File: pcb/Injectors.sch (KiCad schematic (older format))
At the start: 48 parts, among them Q1 VND14NV04, Q2 VND14NV04, Q3 VND14NV04, Q4 VND14NV04, Q5 VND14NV04, Q6 VND14NV04, Q7 VND14NV04, Q8 VND14NV04

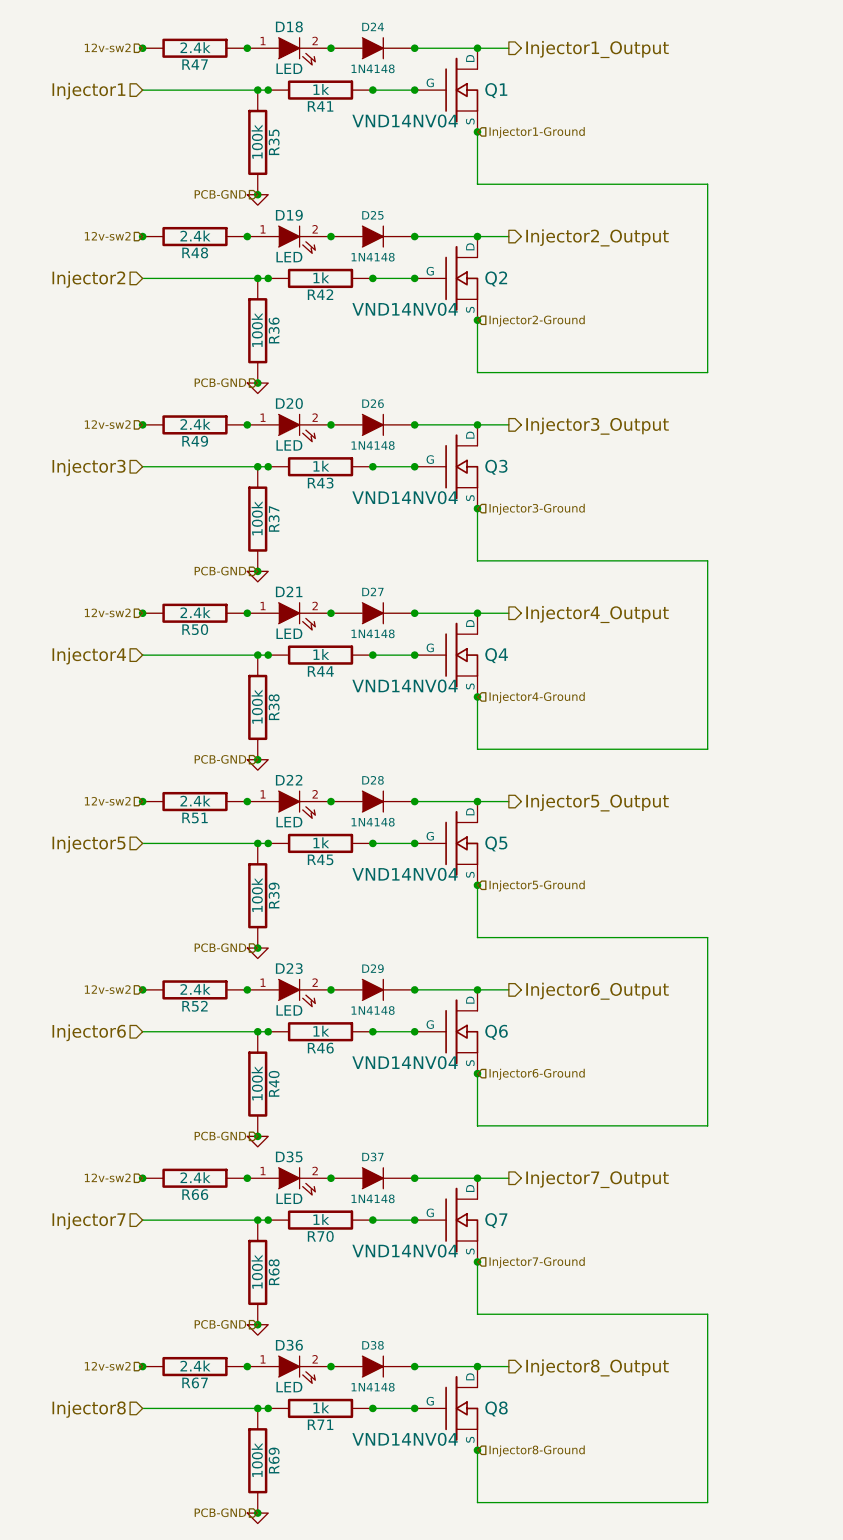
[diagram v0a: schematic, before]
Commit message: Changed ground connection between Q1/Q2 and Q3/Q4 to 0 ohm SMD-1206 jumpers.
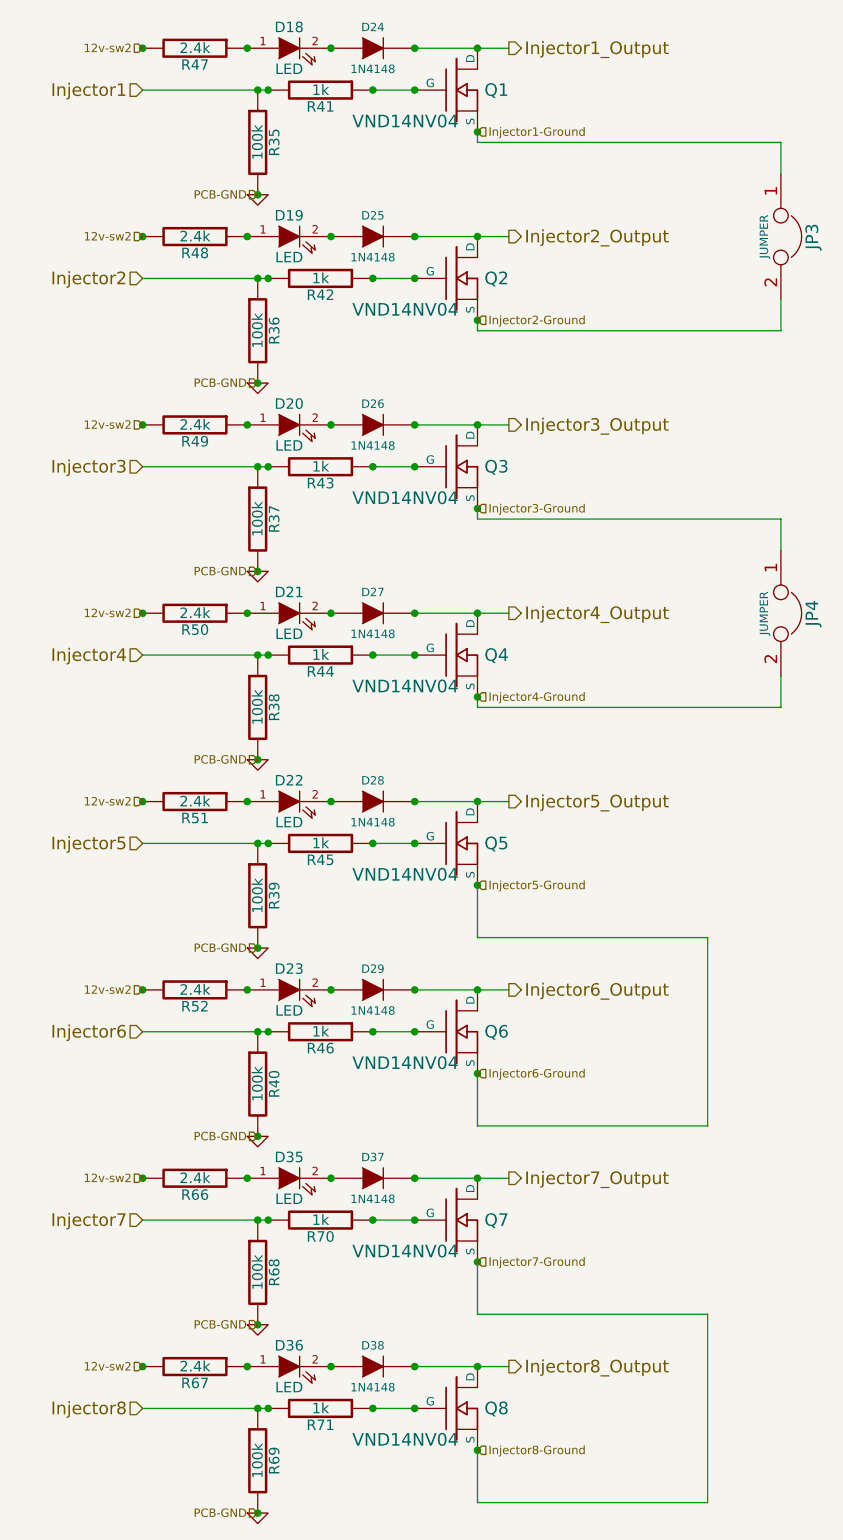
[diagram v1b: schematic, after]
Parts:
- added JP3, JP4: JUMPER, symbol JUMPER
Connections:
- net Injector1-Ground: now also JP3.1; no longer Q2.S
- net Injector3-Ground: now also JP4.1; no longer Q4.S
- new net Injector2-Ground: JP3.2, Q2.S
- new net Injector4-Ground: JP4.2, Q4.S
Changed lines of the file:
@@
-EESchema Schematic File Version 2  date Mon 16 Sep 2013 04:11:09 PM EDT
+EESchema Schematic File Version 2  date Mon 16 Sep 2013 05:06:59 PM EDT
 LIBS:opto
 LIBS:power
@@
 $EndDescr
 Wire Wire Line
+	4000 4700 4000 4950
+Wire Wire Line
+	4000 3800 4000 3850
+Wire Wire Line
+	5450 3700 5450 3850
+Wire Wire Line
+	5450 3850 4000 3850
+Wire Wire Line
+	5450 1900 5450 2050
+Wire Wire Line
+	5450 2050 4000 2050
+Wire Wire Line
+	4000 1100 4000 1150
+Wire Wire Line
 	5100 7650 5100 6750
 Wire Wire Line
-	5100 4050 5100 3150
-Wire Wire Line
 	5100 7650 4000 7650
 Wire Wire Line
@@
 	4000 5850 4000 5600
 Wire Wire Line
-	5100 4050 4000 4050
-Wire Wire Line
-	4000 4050 4000 3800
-Wire Wire Line
-	4000 1100 4000 1350
-Wire Wire Line
-	4000 2000 4000 2250
-Wire Wire Line
-	4000 2250 5100 2250
+	4000 2050 4000 2000
 Connection ~ 3700 7000
 Connection ~ 2950 7700
@@
 Connection ~ 2400 7000
 Wire Wire Line
-	2400 7200 3000 7200
-Wire Wire Line
-	3700 7000 4150 7000
-Wire Wire Line
-	3700 6100 4150 6100
-Wire Wire Line
-	2400 6300 3000 6300
+	3000 7200 2400 7200
+Wire Wire Line
+	4150 7000 3700 7000
+Wire Wire Line
+	4150 6100 3700 6100
+Wire Wire Line
+	3000 6300 2400 6300
 Connection ~ 2400 6100
 Connection ~ 3300 6100
@@
 Connection ~ 3700 6100
 Wire Wire Line
-	3000 1800 2400 1800
-Wire Wire Line
-	2400 900  3000 900
+	2400 1800 3000 1800
+Wire Wire Line
+	3000 900  2400 900
 Connection ~ 3700 5200
 Connection ~ 3700 4300
 Wire Wire Line
-	3700 4300 4150 4300
-Wire Wire Line
-	3700 2500 4150 2500
-Wire Wire Line
-	3000 2700 2400 2700
-Wire Wire Line
-	2400 3600 3000 3600
-Wire Wire Line
-	3000 4500 2400 4500
+	4150 4300 3700 4300
+Wire Wire Line
+	4150 2500 3700 2500
+Wire Wire Line
+	2400 2700 3000 2700
+Wire Wire Line
+	3000 3600 2400 3600
+Wire Wire Line
+	2400 4500 3000 4500
 Connection ~ 4000 700
 Connection ~ 2950 5900
@@
 Connection ~ 2400 5200
 Wire Wire Line
-	2400 5400 3000 5400
+	3000 5400 2400 5400
 Connection ~ 2400 4300
 Connection ~ 2400 3400
 Wire Wire Line
-	3700 3400 4150 3400
+	4150 3400 3700 3400
 Connection ~ 3700 3400
 Connection ~ 3700 2500
 Wire Wire Line
-	3700 700  4150 700
+	4150 700  3700 700
 Connection ~ 2400 700
 Connection ~ 2400 1600
 Connection ~ 2400 2500
 Wire Wire Line
-	3700 5200 4150 5200
-Wire Wire Line
-	3700 1600 4150 1600
-Wire Wire Line
-	4000 1350 5100 1350
-Wire Wire Line
-	4000 2900 4000 3150
-Wire Wire Line
-	4000 3150 5100 3150
-Wire Wire Line
-	4000 4700 4000 4950
+	4150 5200 3700 5200
+Wire Wire Line
+	4150 1600 3700 1600
 Wire Wire Line
 	4000 4950 5100 4950
@@
 	4000 6750 5100 6750
 Wire Wire Line
-	5100 1350 5100 2250
-Wire Wire Line
 	5100 4950 5100 5850
+Wire Wire Line
+	5450 1300 5450 1150
+Wire Wire Line
+	5450 1150 4000 1150
+Wire Wire Line
+	5450 2950 4000 2950
+Wire Wire Line
+	5450 2950 5450 3100
+Wire Wire Line
+	4000 2950 4000 2900
+$Comp
+L JUMPER JP4
+U 1 1 52377227
+P 5450 3400
+F 0 "JP4" H 5450 3550 60  0000 C CNN
+F 1 "JUMPER" H 5450 3320 40  0000 C CNN
+	1    5450 3400
+	0    1    1    0
+$EndComp
+$Comp
+L JUMPER JP3
+U 1 1 52377186
+P 5450 1600
+F 0 "JP3" H 5450 1750 60  0000 C CNN
+F 1 "JUMPER" H 5450 1520 40  0000 C CNN
+	1    5450 1600
+	0    1    1    0
+$EndComp
 Text HLabel 4000 7400 2    40   Input ~ 0
 Injector8-Ground

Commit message: Modified ground jumpers to be 7 jumpers size SMD 2512.
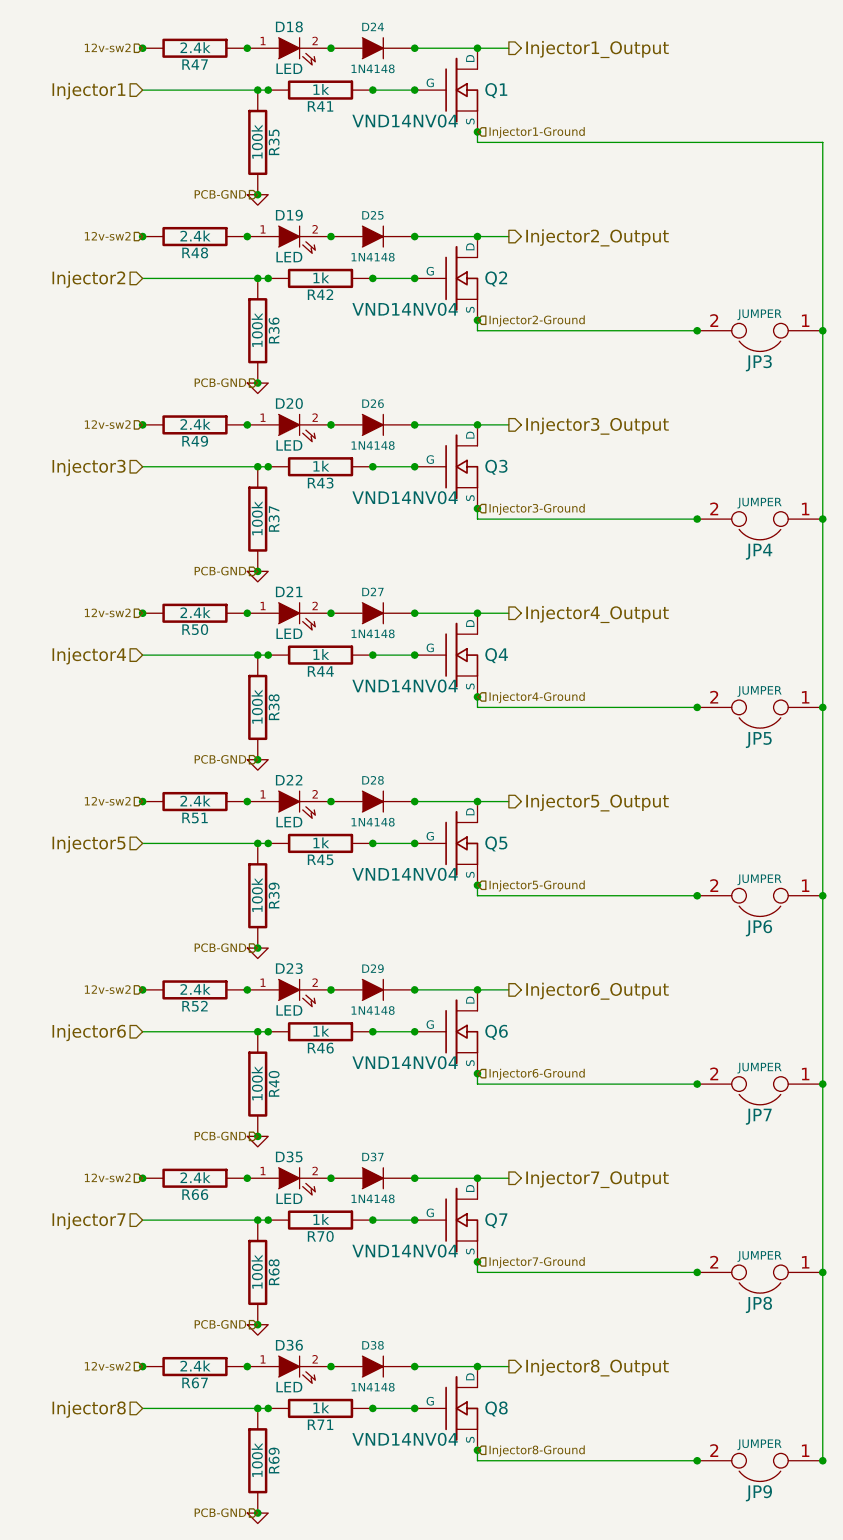
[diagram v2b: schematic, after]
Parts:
- added JP5, JP6, JP7, JP8, JP9: JUMPER, symbol JUMPER
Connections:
- net Injector1-Ground: now also JP4.1, JP5.1, JP6.1, JP7.1, JP8.1, JP9.1
- net Injector3-Ground: now also JP4.2; no longer JP4.1
- net Injector4-Ground: now also JP5.2; no longer JP4.2
- net Injector5-Ground: now also JP6.2; no longer Q6.S
- net Injector7-Ground: now also JP8.2; no longer Q8.S
- new net Injector6-Ground: JP7.2, Q6.S
- new net Injector8-Ground: JP9.2, Q8.S
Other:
- moved on the sheet: JP3, JP4
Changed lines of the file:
@@
-EESchema Schematic File Version 2  date Mon 16 Sep 2013 05:06:59 PM EDT
+EESchema Schematic File Version 2  date Mon 16 Sep 2013 06:18:12 PM EDT
 LIBS:opto
 LIBS:power
@@
 $EndDescr
 Wire Wire Line
-	4000 4700 4000 4950
-Wire Wire Line
-	4000 3800 4000 3850
-Wire Wire Line
-	5450 3700 5450 3850
-Wire Wire Line
-	5450 3850 4000 3850
-Wire Wire Line
-	5450 1900 5450 2050
-Wire Wire Line
-	5450 2050 4000 2050
-Wire Wire Line
-	4000 1100 4000 1150
-Wire Wire Line
-	5100 7650 5100 6750
-Wire Wire Line
-	5100 7650 4000 7650
-Wire Wire Line
-	4000 7650 4000 7400
-Wire Wire Line
-	4000 5850 5100 5850
-Wire Wire Line
-	4000 5850 4000 5600
-Wire Wire Line
-	4000 2050 4000 2000
+	5050 3850 4000 3850
+Connection ~ 5650 3850
+Connection ~ 5050 3850
+Connection ~ 5650 4750
+Connection ~ 5050 4750
+Connection ~ 5050 5650
+Connection ~ 5650 5650
+Connection ~ 5650 6550
+Connection ~ 5050 6550
+Wire Wire Line
+	5050 5650 4000 5650
+Connection ~ 5650 2950
+Connection ~ 5050 2950
+Connection ~ 5050 2050
+Wire Wire Line
+	5050 2950 4000 2950
+Connection ~ 5650 7450
+Connection ~ 5050 7450
+Wire Wire Line
+	5050 7450 4000 7450
+Wire Wire Line
+	4000 1150 5650 1150
+Wire Wire Line
+	4000 6500 4000 6550
+Wire Wire Line
+	4000 4700 4000 4750
+Wire Wire Line
+	4000 3850 4000 3800
+Wire Wire Line
+	4000 1150 4000 1100
+Wire Wire Line
+	4000 2000 4000 2050
 Connection ~ 3700 7000
 Connection ~ 2950 7700
@@
 	4150 1600 3700 1600
 Wire Wire Line
-	4000 4950 5100 4950
-Wire Wire Line
-	4000 6500 4000 6750
-Wire Wire Line
-	4000 6750 5100 6750
-Wire Wire Line
-	5100 4950 5100 5850
-Wire Wire Line
-	5450 1300 5450 1150
-Wire Wire Line
-	5450 1150 4000 1150
-Wire Wire Line
-	5450 2950 4000 2950
-Wire Wire Line
-	5450 2950 5450 3100
-Wire Wire Line
 	4000 2950 4000 2900
+Wire Wire Line
+	4000 5650 4000 5600
+Wire Wire Line
+	4000 7450 4000 7400
+Wire Wire Line
+	5650 1150 5650 7450
+Connection ~ 5650 2050
+Wire Wire Line
+	4000 2050 5050 2050
+Wire Wire Line
+	4000 6550 5050 6550
+Wire Wire Line
+	4000 4750 5050 4750
+$Comp
+L JUMPER JP9
+U 1 1 5237813C
+P 5350 7450
+F 0 "JP9" H 5350 7600 60  0000 C CNN
+F 1 "JUMPER" H 5350 7370 40  0000 C CNN
+	1    5350 7450
+	-1   0    0    1
+$EndComp
+$Comp
+L JUMPER JP8
+U 1 1 52378132
+P 5350 6550
+F 0 "JP8" H 5350 6700 60  0000 C CNN
+F 1 "JUMPER" H 5350 6470 40  0000 C CNN
+	1    5350 6550
+	-1   0    0    1
+$EndComp
+$Comp
+L JUMPER JP7
+U 1 1 52378126
+P 5350 5650
+F 0 "JP7" H 5350 5800 60  0000 C CNN
+F 1 "JUMPER" H 5350 5570 40  0000 C CNN
+	1    5350 5650
+	-1   0    0    1
+$EndComp
+$Comp
+L JUMPER JP6
+U 1 1 5237811B
+P 5350 4750
+F 0 "JP6" H 5350 4900 60  0000 C CNN
+F 1 "JUMPER" H 5350 4670 40  0000 C CNN
+	1    5350 4750
+	-1   0    0    1
+$EndComp
+$Comp
+L JUMPER JP5
+U 1 1 52378114
+P 5350 3850
+F 0 "JP5" H 5350 4000 60  0000 C CNN
+F 1 "JUMPER" H 5350 3770 40  0000 C CNN
+	1    5350 3850
+	-1   0    0    1
+$EndComp
 $Comp
 L JUMPER JP4
 U 1 1 52377227
-P 5450 3400
-F 0 "JP4" H 5450 3550 60  0000 C CNN
-F 1 "JUMPER" H 5450 3320 40  0000 C CNN
-	1    5450 3400
-	0    1    1    0
+P 5350 2950
+F 0 "JP4" H 5350 3100 60  0000 C CNN
+F 1 "JUMPER" H 5350 2870 40  0000 C CNN
+	1    5350 2950
+	-1   0    0    1
 $EndComp
 $Comp
 L JUMPER JP3
 U 1 1 52377186
-P 5450 1600
-F 0 "JP3" H 5450 1750 60  0000 C CNN
-F 1 "JUMPER" H 5450 1520 40  0000 C CNN
-	1    5450 1600
-	0    1    1    0
+P 5350 2050
+F 0 "JP3" H 5350 2200 60  0000 C CNN
+F 1 "JUMPER" H 5350 1970 40  0000 C CNN
+	1    5350 2050
+	-1   0    0    1
 $EndComp
 Text HLabel 4000 7400 2    40   Input ~ 0

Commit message: Rotated ground jumpers 90 degrees and shortened the traces.
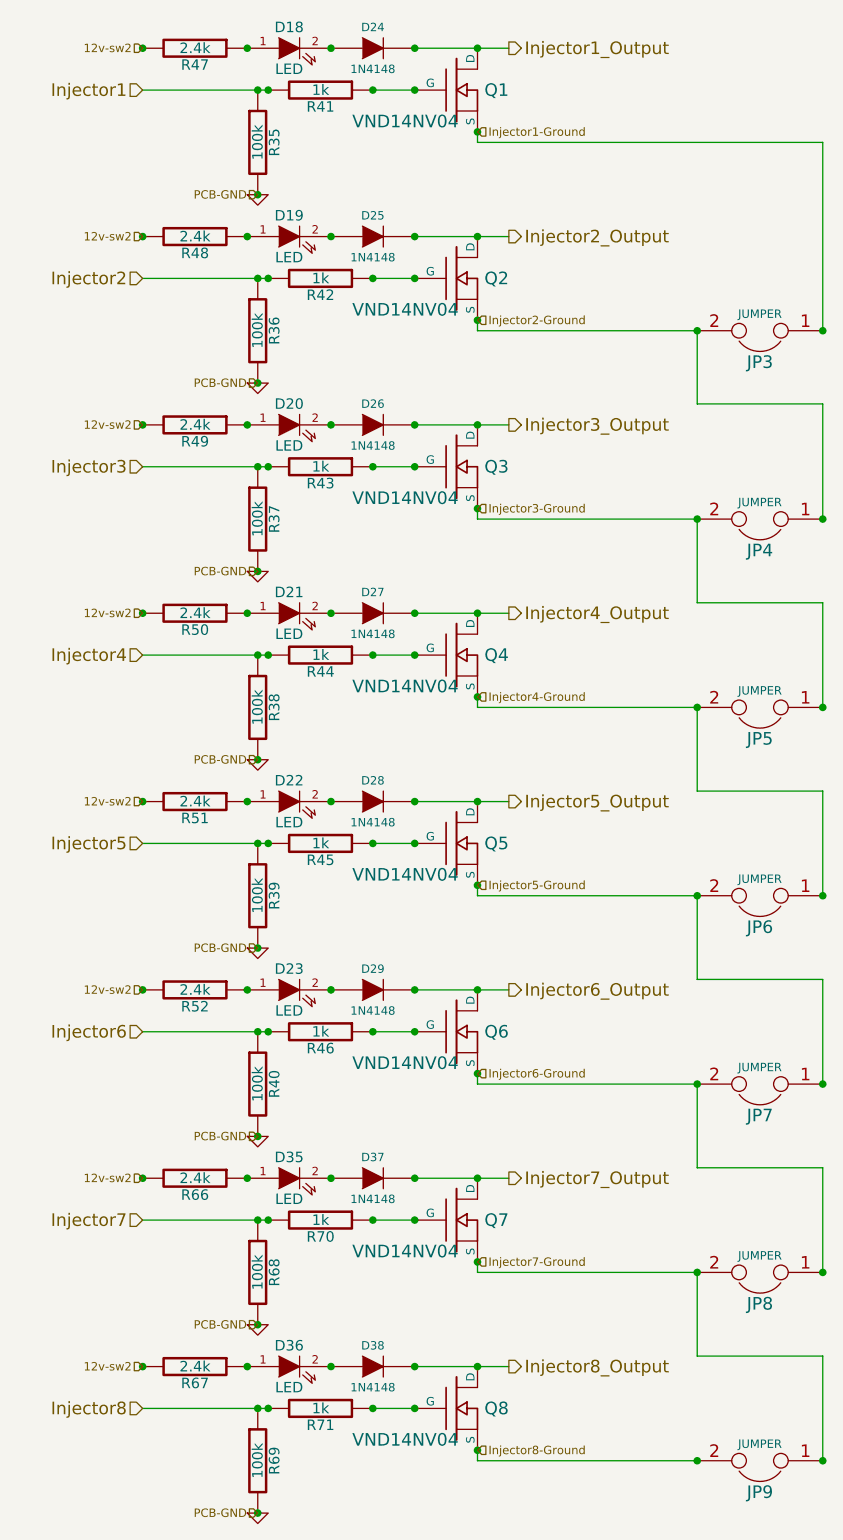
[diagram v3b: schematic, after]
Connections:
- net Injector1-Ground: no longer JP4.1, JP5.1, JP6.1, JP7.1, JP8.1, JP9.1
- net Injector2-Ground: now also JP4.1
- net Injector3-Ground: now also JP5.1
- net Injector4-Ground: now also JP6.1
- net Injector5-Ground: now also JP7.1
- net Injector6-Ground: now also JP8.1
- net Injector7-Ground: now also JP9.1
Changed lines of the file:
@@
-EESchema Schematic File Version 2  date Mon 16 Sep 2013 06:18:12 PM EDT
+EESchema Schematic File Version 2  date Mon 16 Sep 2013 07:56:40 PM EDT
 LIBS:opto
 LIBS:power
@@
 $EndDescr
 Wire Wire Line
+	5650 7450 5650 6950
+Wire Wire Line
+	5650 6950 5050 6950
+Wire Wire Line
+	5050 6950 5050 6550
+Wire Wire Line
+	5650 5650 5650 5150
+Wire Wire Line
+	5650 5150 5050 5150
+Wire Wire Line
+	5050 5150 5050 4750
+Wire Wire Line
+	5050 4250 5650 4250
+Wire Wire Line
+	5050 4250 5050 3850
+Wire Wire Line
+	5650 2950 5650 2400
+Wire Wire Line
+	5650 2400 5050 2400
+Wire Wire Line
+	5050 2400 5050 2050
+Wire Wire Line
 	5050 3850 4000 3850
 Connection ~ 5650 3850
@@
 Connection ~ 5050 6550
 Wire Wire Line
-	5050 5650 4000 5650
+	4000 5650 5050 5650
 Connection ~ 5650 2950
 Connection ~ 5050 2950
 Connection ~ 5050 2050
 Wire Wire Line
-	5050 2950 4000 2950
+	4000 2950 5050 2950
 Connection ~ 5650 7450
 Connection ~ 5050 7450
@@
 	4000 7450 4000 7400
 Wire Wire Line
-	5650 1150 5650 7450
+	5650 1150 5650 2050
 Connection ~ 5650 2050
 Wire Wire Line
@@
 Wire Wire Line
 	4000 4750 5050 4750
+Wire Wire Line
+	5050 2950 5050 3350
+Wire Wire Line
+	5050 3350 5650 3350
+Wire Wire Line
+	5650 3350 5650 3850
+Wire Wire Line
+	5650 4250 5650 4750
+Wire Wire Line
+	5050 5650 5050 6050
+Wire Wire Line
+	5050 6050 5650 6050
+Wire Wire Line
+	5650 6050 5650 6550
 $Comp
 L JUMPER JP9
